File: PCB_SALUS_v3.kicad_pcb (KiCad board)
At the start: 4 copper layers, 100 x 100 mm, 100 parts, among them J1 Debug_U0, J10 RELES_2, J11 Throttle, J12 I2C_EXT1, J13 I2C_EXT2, J14 S_HALL, J15 RF_PPM, J16 USB_NATIVO, J17 SERVO2, J18 SERVO1, J19 +7V_IN, J2 S_GIRO, J3 USB_UART0, J4 Uart1, J5 5V_IN, J6 IBT_2, J7 FC1, J8 FC2, J9 RELES_1, Q3 SS8050, Q4 SS8050, U3 CP2102N-A02-GQFN24, U4 BMI088, U5 74HC595, U6 ULN2003A, U7 LM358, U8 ESP32-S3-WROOM-1, U9 AP63203WU

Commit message: routing
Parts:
- added J20: 3V_IN, Connector_PinHeader_2.54mm:PinHeader_1x02_P2.54mm_Vertical, F.Cu at (96.7, 60.2)
- added R37: 0, Resistor_SMD:R_0805_2012Metric, F.Cu at (104.5, 65.7)
- added R38: 0, Resistor_SMD:R_0805_2012Metric, F.Cu at (111.3, 69.0)
- R2, R3: value R -> 4.7k
- moved C16 228.0 mm to (58.9, 78.5), turned to -90 degrees
- moved C15 201.4 mm to (56.9, 78.7), turned to 90 degrees
- moved U7 193.3 mm to (79.5, 93.0)
- moved C14 190.0 mm to (95.0, 107.6)
- moved U4 179.4 mm to (100.2, 108.5)
- moved R2 172.7 mm to (83.4, 141.2)
- moved R3 172.4 mm to (83.5, 139.5)
- moved U5 171.3 mm to (102.3, 95.2)
- moved C18 165.9 mm to (85.8, 137.8), turned to 90 degrees
- moved C17 165.6 mm to (86.4, 142.1), turned to -90 degrees
- moved U6 165.4 mm to (116.8, 95.2)
- moved R14 164.5 mm to (95.9, 109.8)
- moved FB1 161.1 mm to (95.0, 105.3), turned to 180 degrees
- moved D2 159.7 mm to (62.0, 123.0)
- moved R13 158.0 mm to (101.6, 104.8), turned to -90 degrees
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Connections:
- net /ESP32/USB2_DM renamed /ESP32/USB2_D-
- net /ESP32/USB2_DP renamed /ESP32/USB2_D+
- net /ESP32/USB_DM renamed /ESP32/USB_D-
- net /ESP32/USB_DP renamed /ESP32/USB_D+
- C30 pad 1: +3.3V -> /ALIMENTACION/BUCK_3.3V
- C31 pad 1: +3.3V -> /ALIMENTACION/BUCK_3.3V
- L2 pad 2: +3.3V -> /ALIMENTACION/BUCK_3.3V
- U9 pad 1: +3.3V -> /ALIMENTACION/BUCK_3.3V
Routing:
- net +3.3V: track 0.00 -> 216.1 mm, vias 0 -> 8
- net USB2_VBUS: track 0.00 -> 128.6 mm, vias 0 -> 3
- net /ESP32/RESET: track 0.00 -> 124.2 mm, vias 0 -> 4
- net +5V: track 0.00 -> 124.2 mm, vias 0 -> 3
- net FC_LEFT: track 0.00 -> 111.9 mm, vias 0 -> 2
- net R_PWM: track 0.00 -> 110.4 mm, vias 0 -> 2
- net FC_RIGHT: track 0.00 -> 108.5 mm, vias 0 -> 2
- net HBRIDGE_EN: track 0.00 -> 108.2 mm, vias 0 -> 2
- net L_PWM: track 0.00 -> 106.1 mm, vias 0 -> 2
- net I2C_SDA: track 0.00 -> 101.6 mm, vias 0 -> 2
- net I2C_SCL: track 0.00 -> 97.0 mm, vias 0 -> 2
- net /ESP32/BOOT: track 0.00 -> 91.6 mm, vias 0 -> 4
- net HALL_A: track 0.00 -> 89.4 mm, vias 0 -> 2
- net /ESP32/U1_TX: track 0.00 -> 89.0 mm, vias 0 -> 4
- net HALL_B: track 0.00 -> 88.8 mm, vias 0 -> 2
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- removed copper zone on In1.Cu, net GND
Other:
- copper layers 4 -> 2

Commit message: routeo terminado v1
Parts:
- moved R19 213.8 mm to (57.0, 69.2), turned to -90 degrees
- moved R36 192.8 mm to (71.0, 133.7), turned to -90 degrees
- moved R18 191.9 mm to (72.8, 91.5), turned to 180 degrees
- moved C20 184.9 mm to (72.6, 93.9), turned to 180 degrees
- moved R12 182.0 mm to (73.7, 135.0), turned to -90 degrees
- moved R20 174.7 mm to (85.1, 133.4), turned to 180 degrees
- moved C21 173.4 mm to (85.3, 92.8), turned to -90 degrees
- moved R11 170.6 mm to (85.1, 135.0), turned to 180 degrees
- moved R35 167.4 mm to (96.8, 119.8), turned to -90 degrees
- moved R17 165.1 mm to (95.1, 119.8), turned to 90 degrees
- moved R34 164.5 mm to (101.8, 100.5)
- moved R16 163.3 mm to (101.7, 88.8), turned to 90 degrees
- moved R15 154.1 mm to (106.9, 107.4), turned to -90 degrees
- moved R21 149.3 mm to (114.6, 132.1), turned to 180 degrees
- moved R24 139.9 mm to (123.9, 132.3)
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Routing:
- net Net-(J18-Pin_3): track 0.00 -> 148.8 mm, vias 0 -> 4
- net Net-(J17-Pin_3): track 0.00 -> 143.3 mm, vias 0 -> 4
- net +5V: track 124.2 -> 229.2 mm, vias 3 -> 8
- net +3.3V: track 216.1 -> 319.7 mm, vias 8 -> 12
- net RELAY_OE: track 0.00 -> 71.9 mm, vias 0 -> 6
- net USB_VBUS: track 22.3 -> 93.6 mm, vias 2 -> 7
- net GND: track 0.00 -> 65.5 mm, vias 0 -> 18
- net I2C_SDA: track 101.6 -> 166.0 mm, vias 2 -> 4
- net +7V: track 0.00 -> 64.2 mm, vias 0 -> 4
- net I2C_SCL: track 97.0 -> 154.4 mm, vias 2 -> 6
- net RELAY_LATCH: track 0.00 -> 56.8 mm, vias 0 -> 4
- net Net-(J9-Pin_2): track 0.00 -> 51.8 mm, vias 0 -> 4
- net Net-(U7A-+): track 0.00 -> 49.1 mm, vias 0 -> 6
- net Net-(J15-Pin_3): track 0.00 -> 48.1 mm, vias 0 -> 2
- net /SENSORES/THROTTLE_OUT: track 0.00 -> 42.4 mm, vias 0 -> 2
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- added copper zone on B.Cu, net GND
- added copper zone on F.Cu, net GND

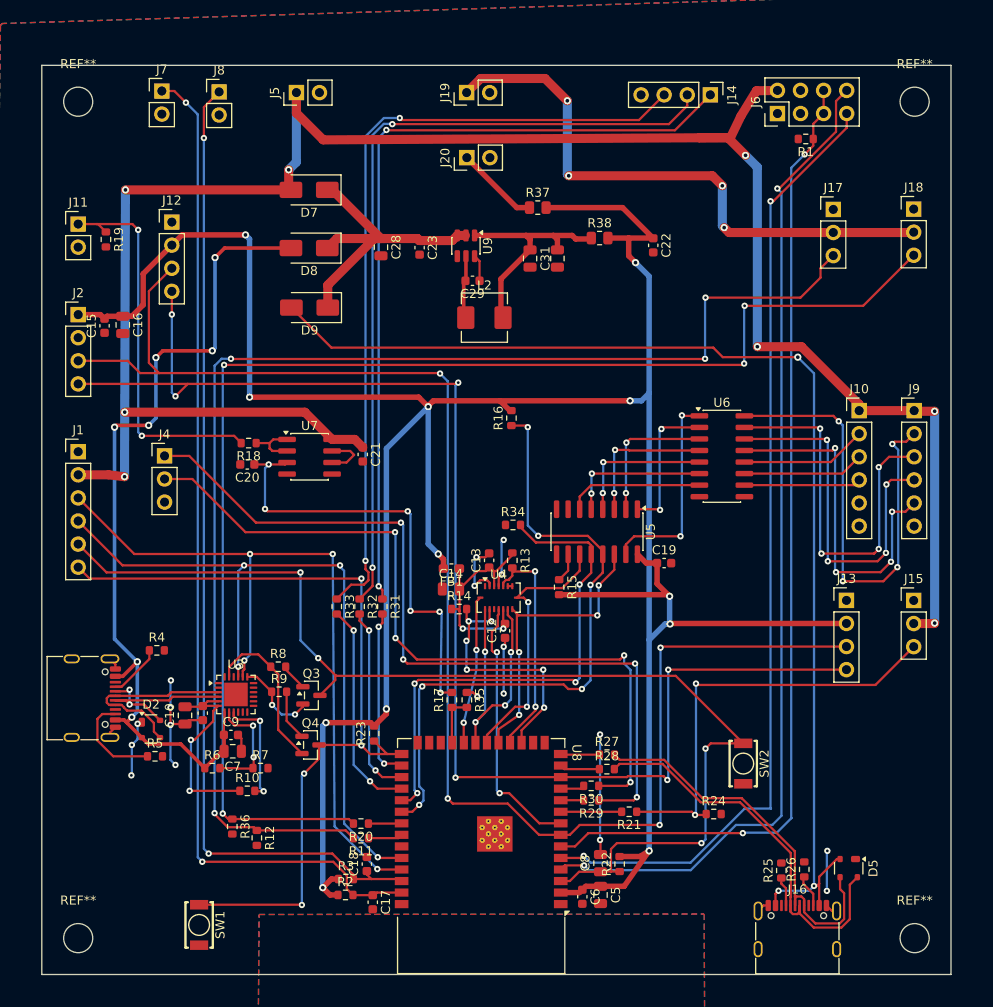
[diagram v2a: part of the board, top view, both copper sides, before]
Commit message: buck remplazado por regulador lineal
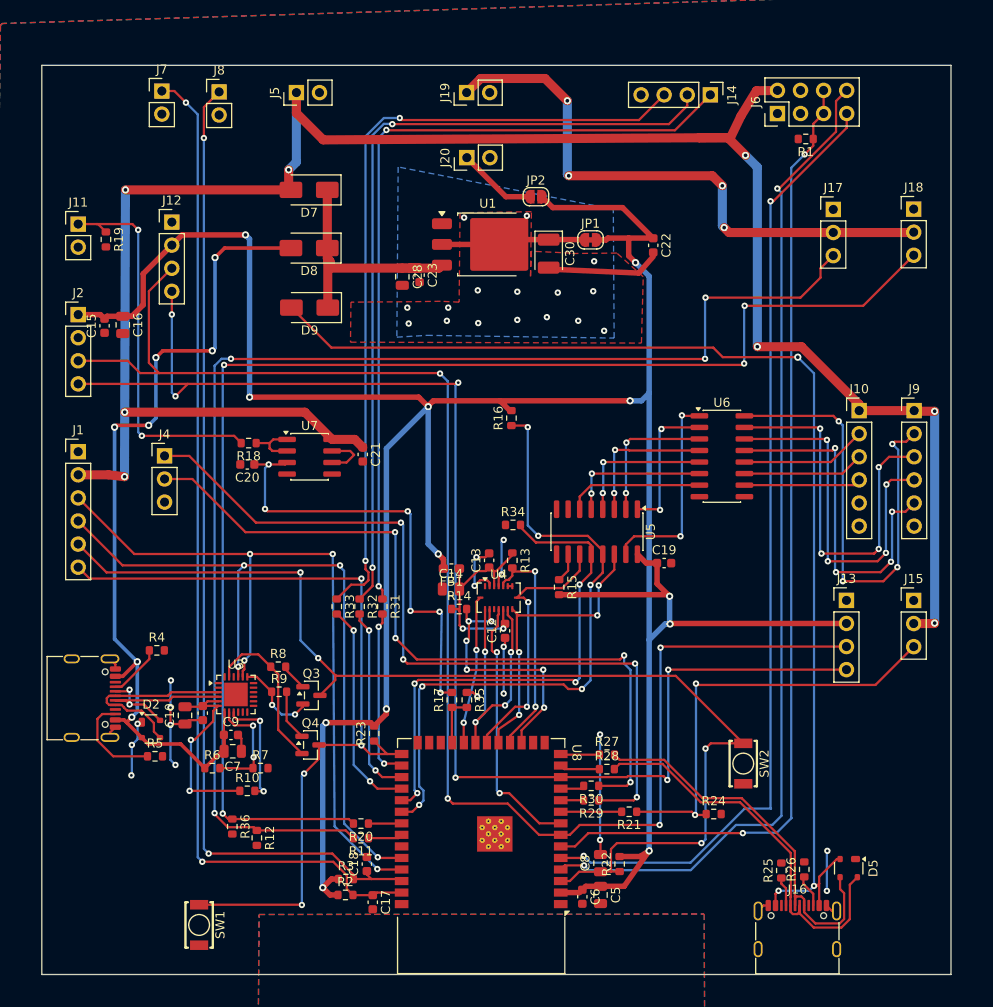
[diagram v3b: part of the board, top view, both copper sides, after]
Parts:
- removed C29: 100nF, Capacitor_SMD:C_0603_1608Metric
- removed C31: 22uF, Capacitor_SMD:C_0805_2012Metric
- removed L2: 4.7uH, Inductor_SMD:L_Changjiang_FXL0530
- removed R37, R38: 0, Resistor_SMD:R_0805_2012Metric
- removed REF** (x4): MountingHole_3.2mm_M3, MountingHole:MountingHole_3.2mm_M3
- removed U9: AP63203WU, Package_TO_SOT_SMD:TSOT-23-6
- added JP1: SolderJumper_2_Bridged, Jumper:SolderJumper-2_P1.3mm_Bridged_RoundedPad1.0x1.5mm, F.Cu at (110.3, 69.2)
- added JP2: SolderJumper_2_Open, Jumper:SolderJumper-2_P1.3mm_Open_RoundedPad1.0x1.5mm, F.Cu at (104.3, 64.5)
- added U1: AMS1117CD-3.3, Package_TO_SOT_SMD:TO-252-3_TabPin2, F.Cu at (99.0, 69.7)
- C30: footprint Capacitor_SMD:C_0805_2012Metric -> Capacitor_Tantalum_SMD:CP_EIA-3528-21_Kemet-B
- moved C28 4.01 mm to (89.7, 73.2)
- moved C23 3.03 mm to (91.5, 73.1)
- moved C30 1.10 mm to (105.8, 70.7)
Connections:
- C30 pad 1: /ALIMENTACION/BUCK_3.3V -> /ALIMENTACION/LINEAR_3.3V
- J20 pad 1: /ALIMENTACION/3.3V_EXT -> Net-(J20-Pin_1)
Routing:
- net /ALIMENTACION/BUCK_3.3V: track 25.5 -> 0.00 mm
- net /ALIMENTACION/LINEAR_3.3V: track 0.00 -> 15.9 mm, vias 0 -> 16
- net GND: track 65.5 -> 78.4 mm
- net /ALIMENTACION/3.3V_EXT: track 9.17 -> 0.00 mm
- net Net-(J20-Pin_1): track 0.00 -> 8.73 mm
- net Net-(U9-SW): track 6.96 -> 0.00 mm
- net 5V_SYS: track 34.5 -> 29.4 mm
- net Net-(U9-BST): track 2.94 -> 0.00 mm
- net +3.3V: track 319.7 -> 322.0 mm
- added copper zone on B.Cu, net /ALIMENTACION/LINEAR_3.3V
- added copper zone on F.Cu, net /ALIMENTACION/LINEAR_3.3V

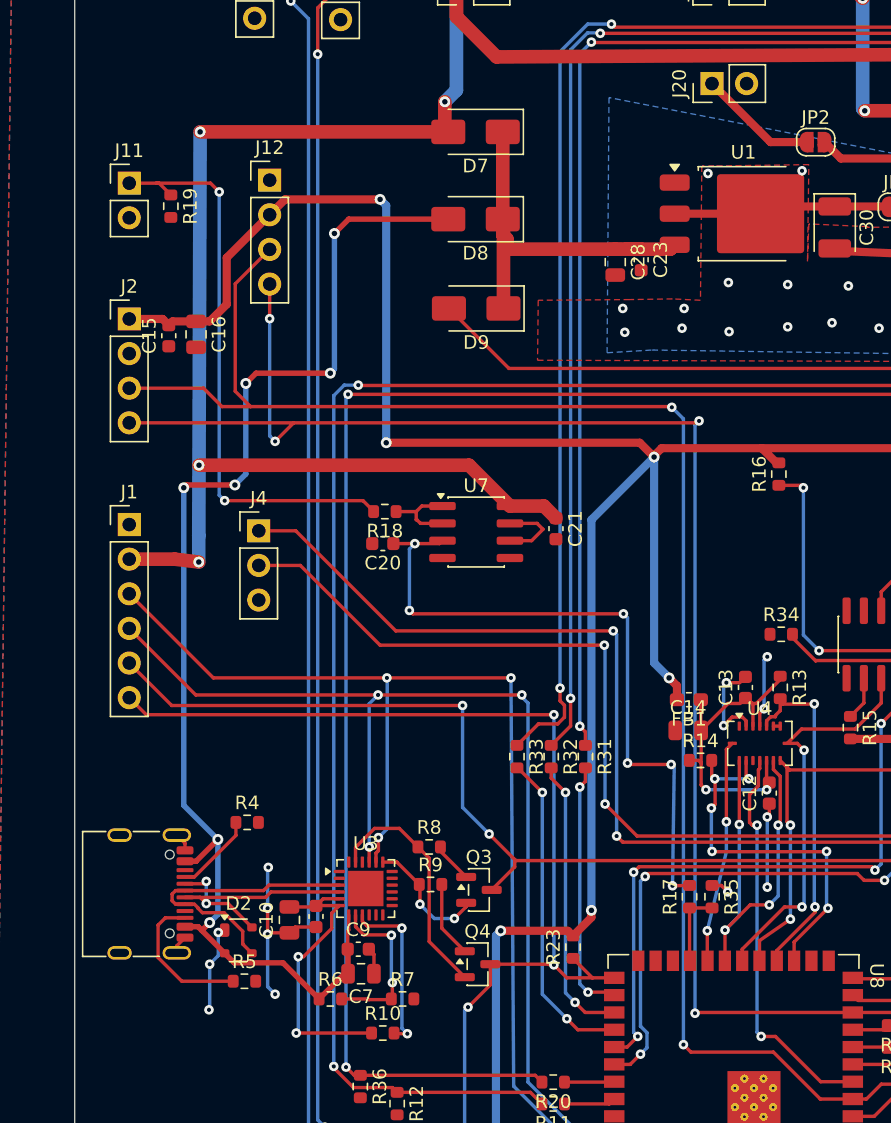
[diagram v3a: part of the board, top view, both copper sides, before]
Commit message: removed usb_uart0
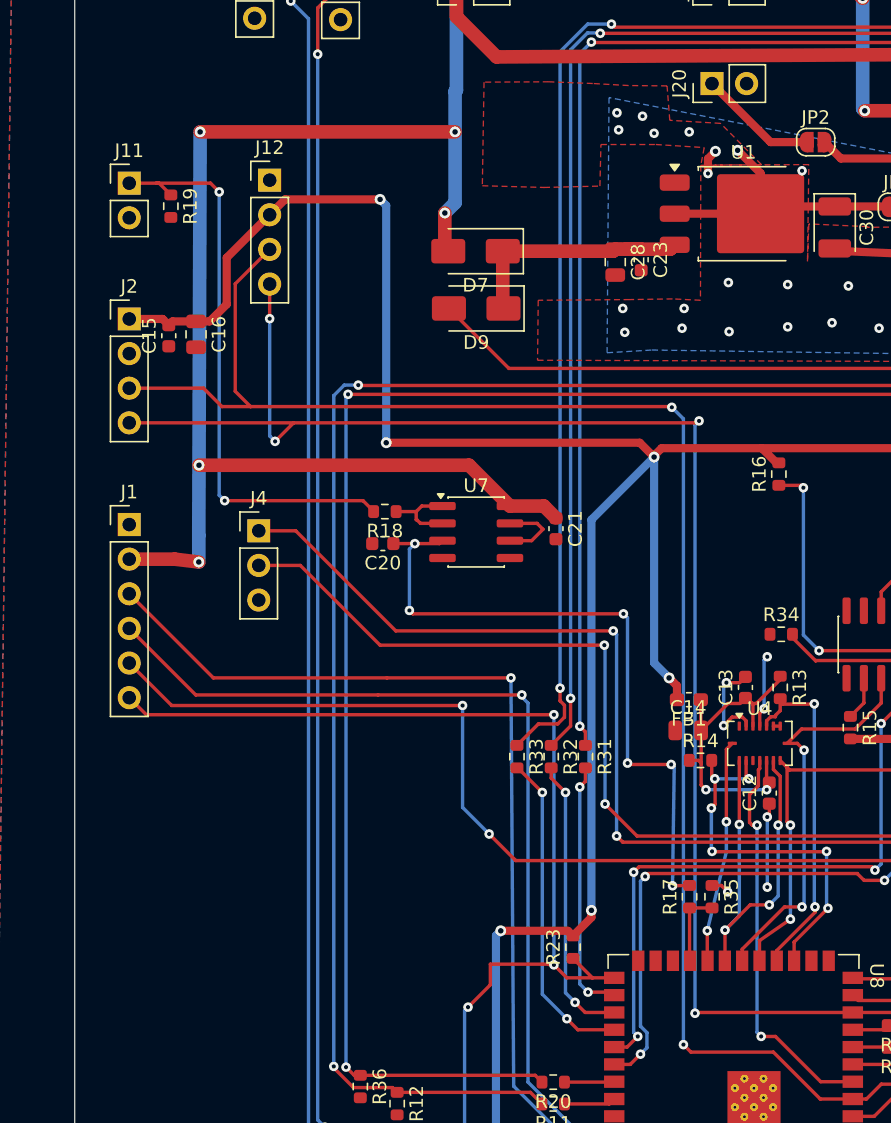
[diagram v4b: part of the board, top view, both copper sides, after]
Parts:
- removed C10, C7: 4.7uF, Capacitor_SMD:C_0805_2012Metric
- removed C11, C9: 100nF, Capacitor_SMD:C_0603_1608Metric
- removed D2: SP0503BAHTG, Package_TO_SOT_SMD:SOT-143
- removed D8: SS14, Diode_SMD:D_SMA
- removed J3: USB_UART0, Connector_USB:USB_C_Receptacle_G-Switch_GT-USB-7010ASV
- removed Q3, Q4: SS8050, Package_TO_SOT_SMD:SOT-23
- removed R10: 1k, Resistor_SMD:R_0603_1608Metric
- removed R4, R5: 5.1k, Resistor_SMD:R_0603_1608Metric
- removed R6: 22.1k, Resistor_SMD:R_0603_1608Metric
- removed R7: 47.5k, Resistor_SMD:R_0603_1608Metric
- removed R8, R9: 10k, Resistor_SMD:R_0603_1608Metric
- removed U3: CP2102N-A02-GQFN24, Package_DFN_QFN:QFN-24-1EP_4x4mm_P0.5mm_EP2.6x2.6mm
- moved D7 8.75 mm to (79.4, 72.5)
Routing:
- net USB_VBUS: track 93.6 -> 0.00 mm, vias 7 -> 0
- net GND: track 78.4 -> 53.9 mm, vias 18 -> 11
- net CP2102_3V3: track 22.0 -> 0.00 mm, vias 2 -> 0
- net /ESP32/USB_D+: track 21.0 -> 0.00 mm
- net /ESP32/USB_D-: track 20.6 -> 0.00 mm, vias 2 -> 0
- net /ESP32/DTR: track 17.8 -> 0.00 mm
- net /ESP32/U0TX: track 83.7 -> 69.8 mm, vias 4 -> 2
- net /ESP32/U0RX: track 79.8 -> 67.3 mm, vias 4 -> 2
- net Net-(U3-~{RST}): track 12.5 -> 0.00 mm, vias 2 -> 0
- net Net-(U3-VBUS): track 12.2 -> 0.00 mm, vias 2 -> 0
- net 5V_SYS: track 29.4 -> 18.1 mm
- net Net-(J3-CC2): track 10.8 -> 0.00 mm
- net /ESP32/RTS: track 9.29 -> 0.00 mm, vias 2 -> 0
- net +5V: track 229.2 -> 238.4 mm, vias 8 -> 9
- net /ALIMENTACION/LINEAR_3.3V: track 15.9 -> 23.1 mm, vias 16 -> 23
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
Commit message: fixes
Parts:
- moved C23 2.68 mm to (93.7, 74.7)
- moved C28 1.97 mm to (91.6, 73.0)
- moved C30 0.25 mm to (105.5, 70.7)
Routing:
- net /ALIMENTACION/LINEAR_3.3V: track 23.1 -> 38.5 mm, vias 23 -> 33
- net 5V_SYS: track 18.1 -> 19.1 mm

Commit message: se hicieron los boom, cpl y gerbers
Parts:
- SW1, SW2: footprint Footprints:Boton_Simple -> Footprints:Switch-Definitivo
- moved SW1 3.87 mm to (64.1, 142.4), turned to 180 degrees
- moved SW2 1.30 mm to (127.2, 125.5)
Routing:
- net /ALIMENTACION/LINEAR_3.3V: track 38.5 -> 15.5 mm, vias 33 -> 32
- net /ESP32/BOOT: track 91.6 -> 94.6 mm
- net /ESP32/RESET: track 121.3 -> 123.3 mm, vias 4 -> 5

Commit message: RS485
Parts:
- added C7: 100nF, Capacitor_SMD:C_0603_1608Metric, F.Cu at (61.0, 126.5)
- added J3: RS485, Connector_PinHeader_2.54mm:PinHeader_1x04_P2.54mm_Vertical, F.Cu at (53.9, 117.1)
- added R37: 10k, Resistor_SMD:R_0603_1608Metric, F.Cu at (71.3, 124.5)
- added U2: SP3485EN, Package_SO:SOIC-8_3.9x4.9mm_P1.27mm, F.Cu at (62.6, 123.0)
- moved R21 5.41 mm to (120.0, 131.5)
- moved R24 3.28 mm to (120.8, 133.2)
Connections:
- R24 pad 1: Net-(J15-Pin_3) -> RF_PPM
- U8 pad 35: unconnected-(U8-IO42-Pad35) -> RS485_DIR
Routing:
- net RS485_DIR: track 0.00 -> 42.2 mm, vias 0 -> 4
- net /ESP32/U1_RX: track 83.7 -> 124.4 mm, vias 4 -> 6
- net /ESP32/U1_TX: track 89.0 -> 121.9 mm, vias 4 -> 6
- net +3.3V: track 322.0 -> 351.9 mm, vias 12 -> 14
- net +5V: track 238.4 -> 264.9 mm, vias 9 -> 10
- net RF_PPM: track 6.70 -> 14.4 mm
- net Net-(J15-Pin_3): track 48.1 -> 40.5 mm
- net /ESP32/RS485_B: track 0.00 -> 6.70 mm
- net /ESP32/RS485_A: track 0.00 -> 6.28 mm

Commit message: RS485 upgrades
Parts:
- added D1: SM712_SOT23, Package_TO_SOT_SMD:SOT-23, F.Cu at (57.8, 119.6)
- added R4: 120, Resistor_SMD:R_0603_1608Metric, F.Cu at (57.2, 123.0)
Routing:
- net /ESP32/RS485_B: track 6.70 -> 14.6 mm
- net /ESP32/RS485_A: track 6.28 -> 11.2 mm
